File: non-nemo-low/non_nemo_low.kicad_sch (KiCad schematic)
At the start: 82 parts, among them J1 Conn_BAT, J2 Conn_BAT

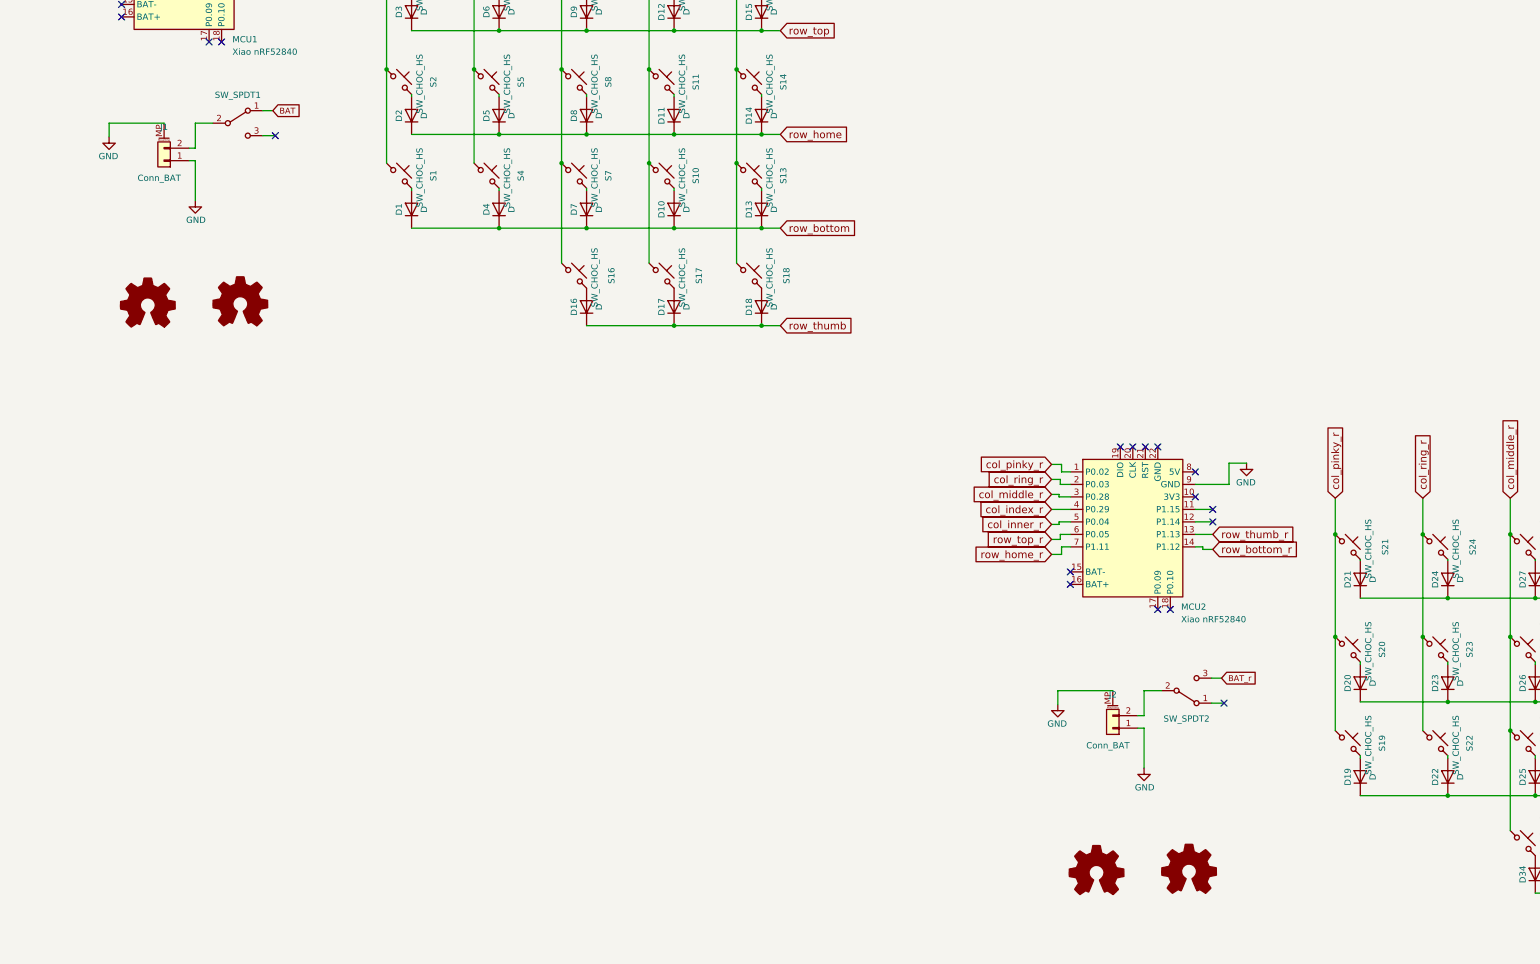
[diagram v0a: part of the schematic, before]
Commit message: Low Profile
pogopin and reset button
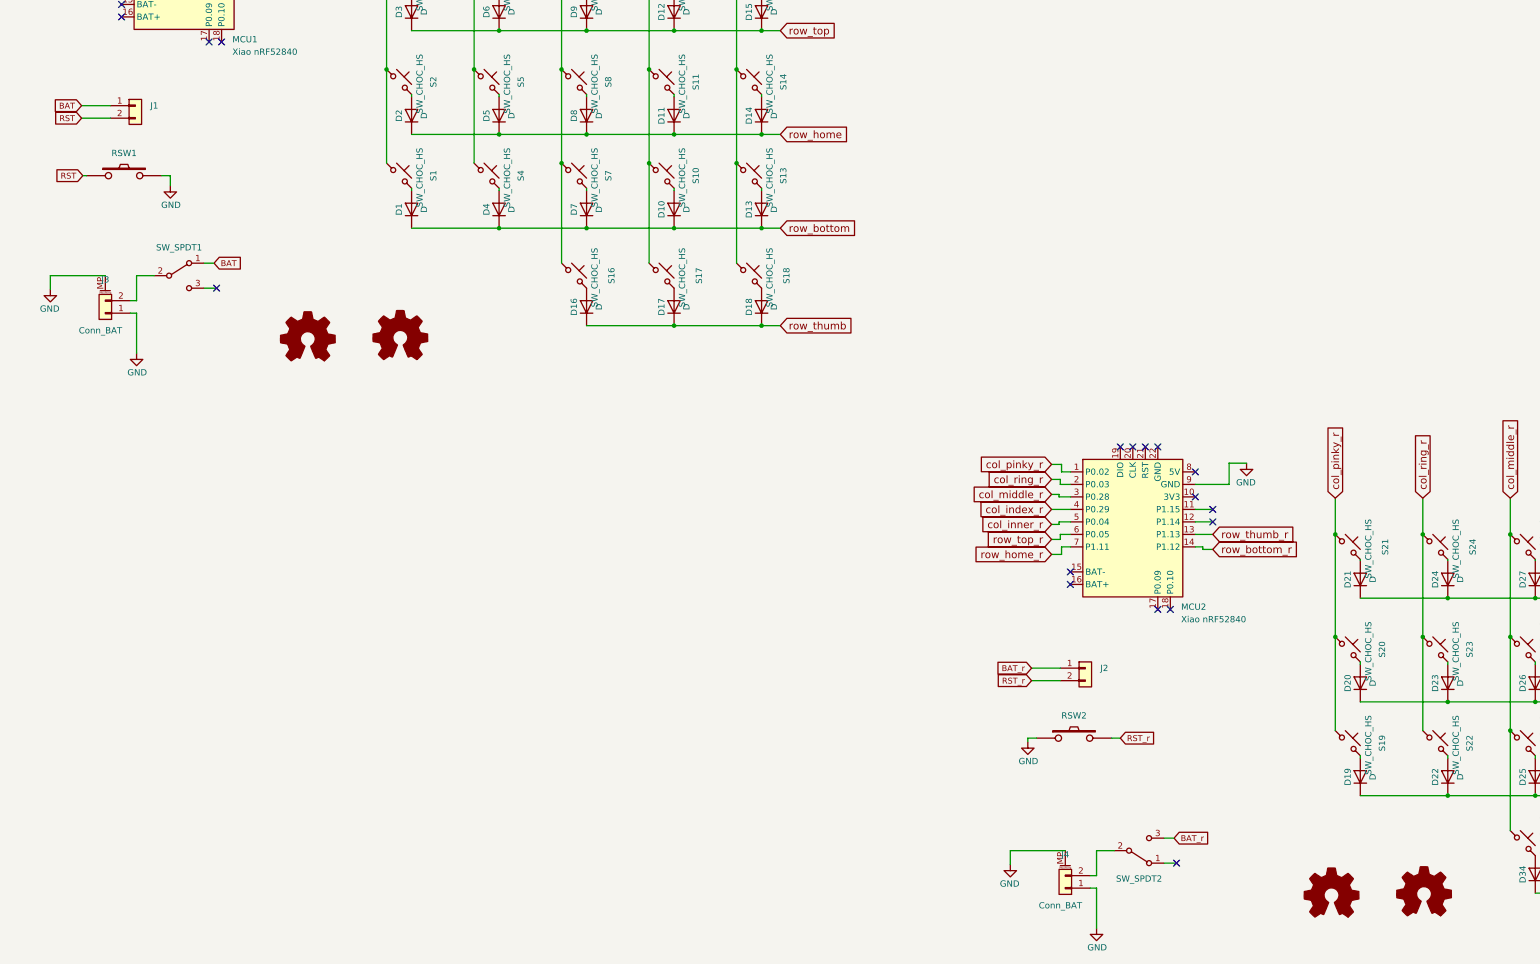
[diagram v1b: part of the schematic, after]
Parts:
- added J1, J2: Conn_01x02, TB2086_MISC:Tag_Pogopin_1x02_P2.54mm, symbol Connector_Generic:Conn_01x02
- added RSW1, RSW2: SMT 2X4X3.5MM Tactile Tact Push Button, TB2086_SMD:SMT 2X4X3.5MM Tactile Tact Push Button, symbol TB2086_SMD:SMT 2X4X3.5MM Tactile Tact Push Button
- renumbered J1 to J3, J2 to J4
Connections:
- net BAT: now also J1.1 (Pin_1)
- net BAT_r: now also J2.1 (Pin_1)
- net GND: now also RSW1.2, RSW2.1
- new net RST: J1.2 (Pin_2), RSW1.1
- new net RST_r: J2.2 (Pin_2), RSW2.2
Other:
- moved on the sheet: J3, J4

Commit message: MX Profile
pogopin and reset switch
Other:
- title: (none) -> Non Nemo Low Profile
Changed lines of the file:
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@@
 	(generator_version "8.0")
 	(paper "A3")
+	(title_block
+		(title "Non Nemo Low Profile")
+		(date "2025-04-09")
+		(rev "0.2.0")
+	)
 	(junction
 		(at 357.378 201.422)
